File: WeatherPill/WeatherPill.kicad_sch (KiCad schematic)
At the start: 24 parts, among them J2 Conn_02x08_Odd_Even, J3 USB4125-GF-A_REVA2, J4 Conn_02x08_Odd_Even, SW1 EVQ-P7A01P, SW2 EVQ-P7A01P, U1 STM32L052K8Tx, U12 USBLC6-2SC6, U13 BU9796AMUV-E2, U14 SHTC3, U2 SHT40-AD1B-R2, U3 BME280, U4 sst25vf512a-33-4c-sae, U7 STTS22HTR

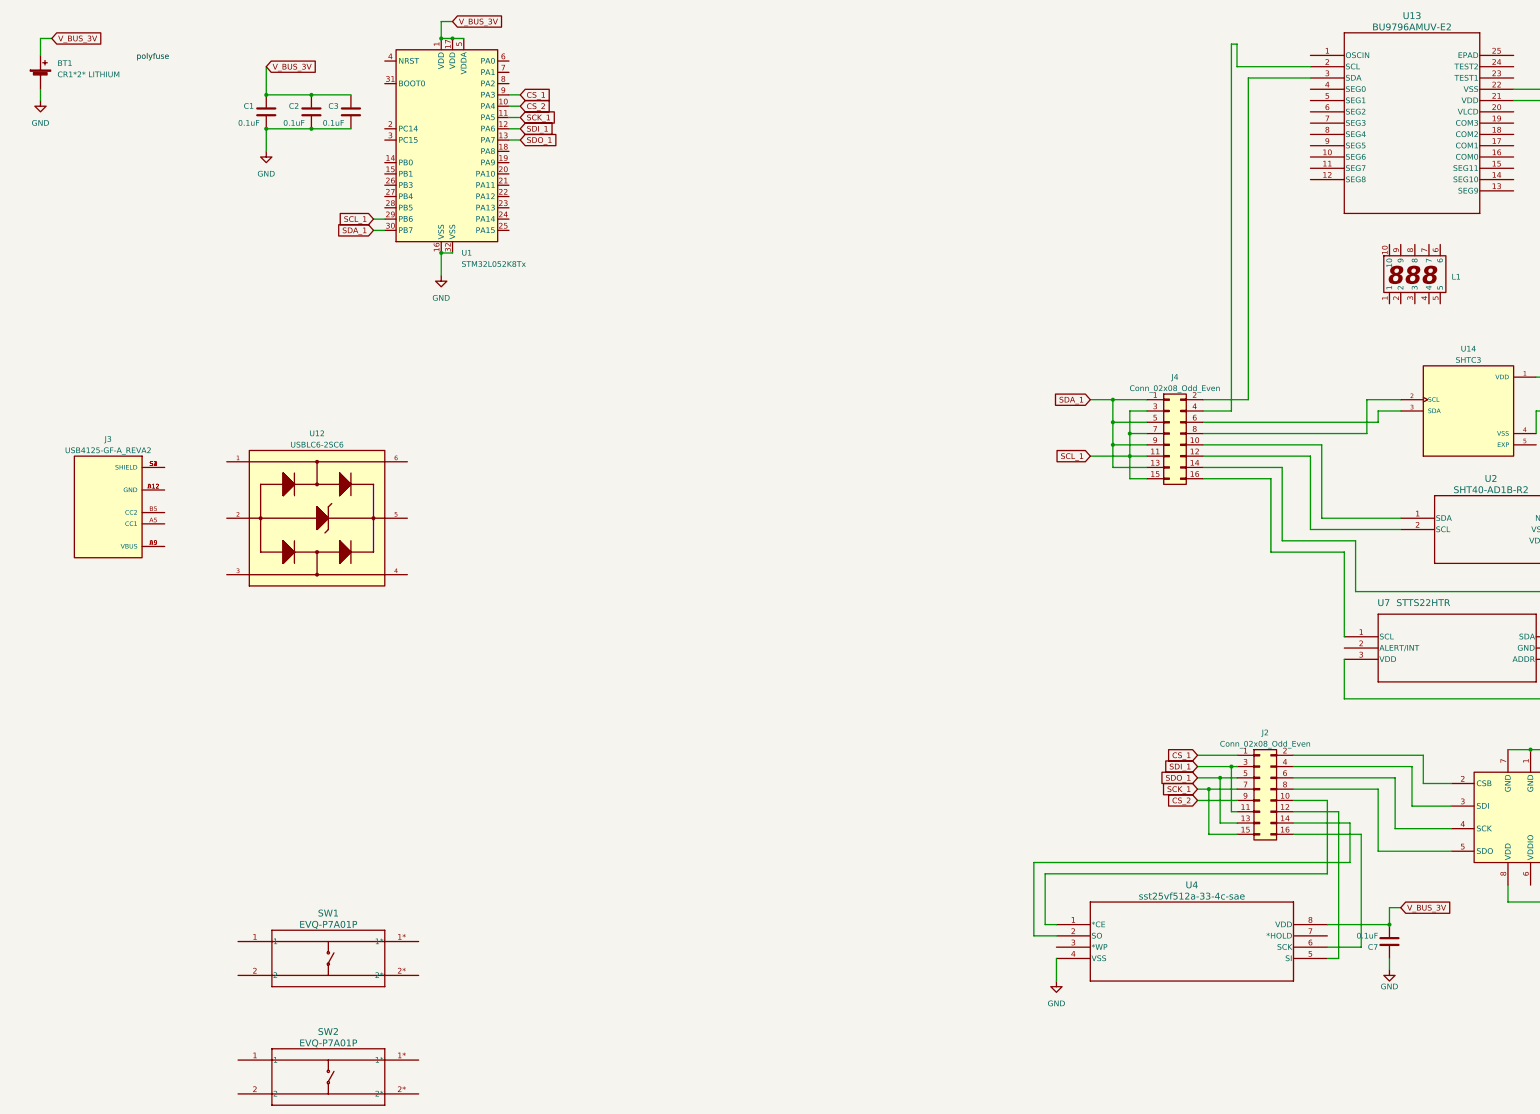
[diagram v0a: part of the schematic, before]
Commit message: stating to configs pins
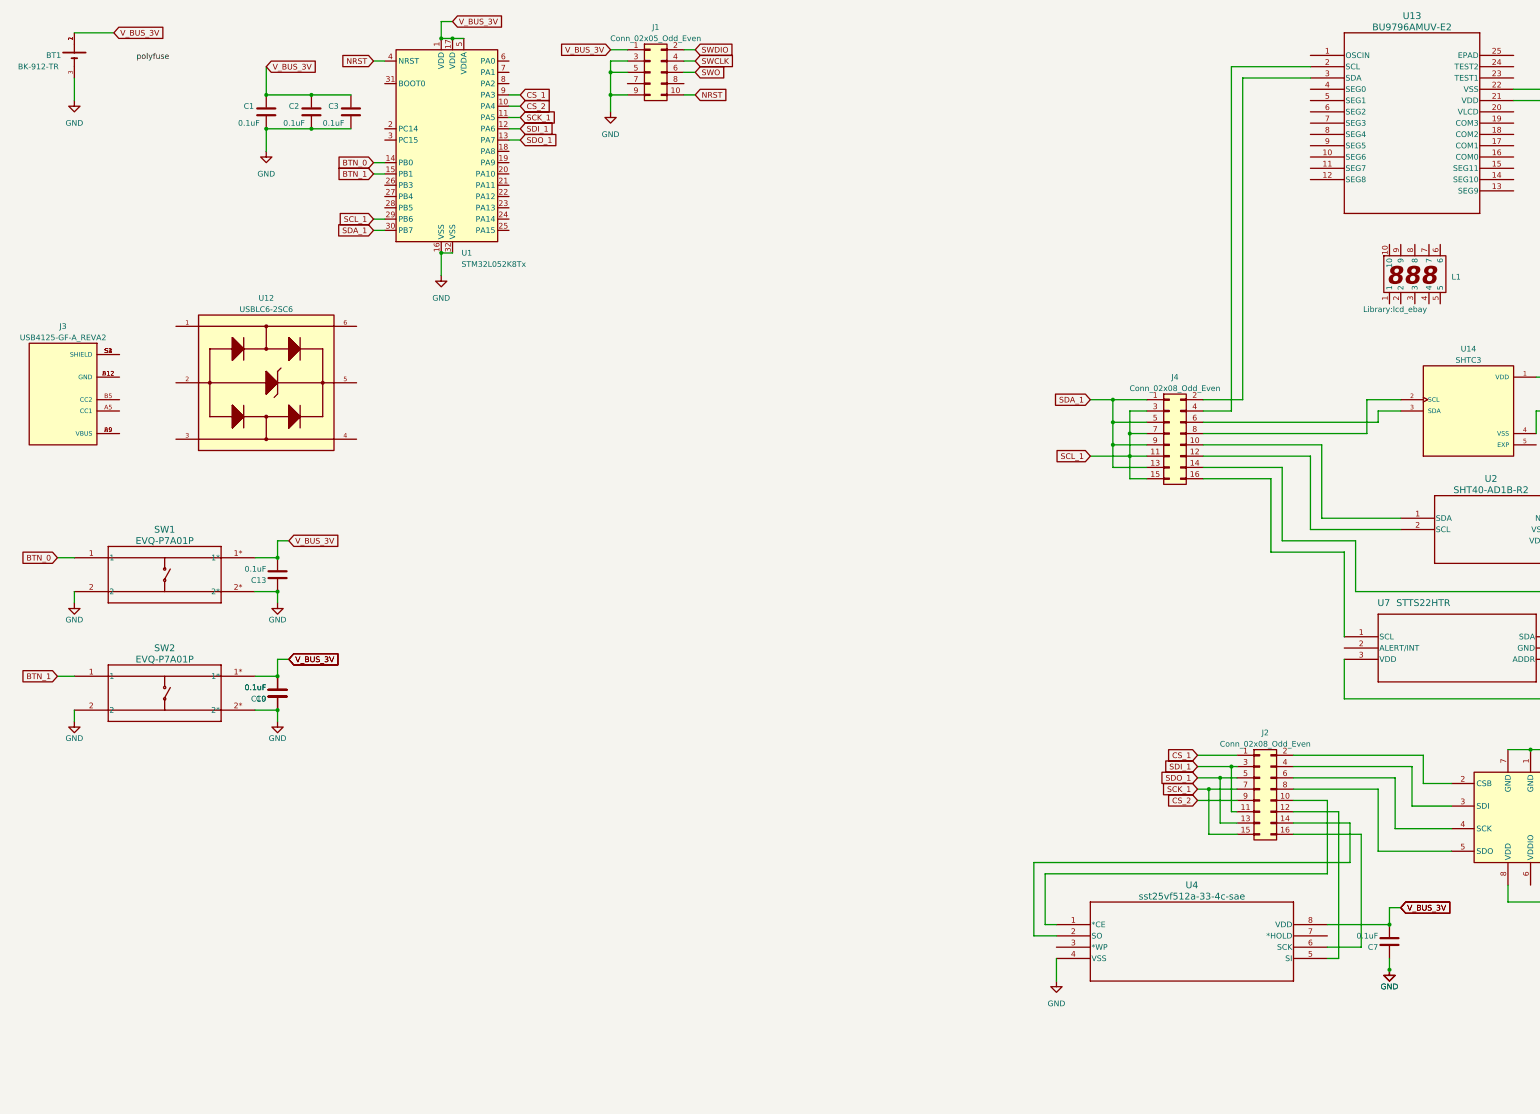
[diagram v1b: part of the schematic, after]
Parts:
- removed BT1: CR1*2* LITHIUM, symbol Device:Battery_Cell
- added BT1: BK-912-TR, MPD_BK-912-TR, symbol BK-912-TR:BK-912-TR
- added C10, C13, C9: 0.1uF, Capacitor_SMD:C_0603_1608Metric_Pad1.08x0.95mm_HandSolder, symbol Device:C
- added J1: Conn_02x05_Odd_Even, symbol Connector_Generic:Conn_02x05_Odd_Even
- L1: footprint (none) -> Library:lcd_ebay
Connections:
- net GND: now also SW1.2, SW1.2*, SW2.2, SW2.2*, BT1.3, C10.1, C13.1, C9.1, J1.3 (Pin_3), J1.5 (Pin_5), J1.9 (Pin_9)
- net V_BUS_3V: now also SW1.1*, SW2.1*, BT1.1, BT1.2, C10.2, C13.2, C9.2, J1.1 (Pin_1)
- net BTN_1: now reaches SW2.1
- net BTN_1: now also U1.15 (PB1)
- net BTN_0: now reaches SW1.1
- net BTN_0: now also U1.14 (PB0)
- net NRST: now reaches U1.4 (NRST)
- net NRST: now also J1.10 (Pin_10)
- new net SWCLK: J1.4 (Pin_4)
- new net SWDIO: J1.2 (Pin_2)
- new net SWO: J1.6 (Pin_6)
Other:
- moved on the sheet: J3, SW1, SW2, U12

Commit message: in review
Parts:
- removed C5, C9: 0.1uF, Capacitor_SMD:C_0603_1608Metric_Pad1.08x0.95mm_HandSolder, symbol Device:C
- removed J3: USB4125-GF-A_REVA2, GCT_USB4125-GF-A_REVA2, symbol usb_CONN:USB4125-GF-A_REVA2
- removed U12: USBLC6-2SC6, SOT95P280X145-6N, symbol tvs:USBLC6-2SC6
- removed U7: STTS22HTR, UDFN-6L_2X2X0P5_STM, symbol STTS22HTR:STTS22HTR
- added C8: 100nF, Capacitor_SMD:C_0603_1608Metric_Pad1.08x0.95mm_HandSolder, symbol Device:C
- added H1, H2, H3, H4: MountingHole, MountingHole:MountingHole_3.2mm_M3_DIN965, symbol Mechanical:MountingHole
- added J3: 12402012E212A, usb conn:12402012E212A_AMP, symbol usb conn:12402012E212A
- added J5: Conn_01x02_Pin, Connector_PinHeader_2.54mm:PinHeader_1x02_P2.54mm_Vertical, symbol Connector:Conn_01x02_Pin
- added Q1, Q2, Q3: PMOS, Package_TO_SOT_SMD:SOT-323_SC-70_Handsoldering, symbol Simulation_SPICE:PMOS
- added R1, R2, R7, R8, R9: 1M, Capacitor_SMD:C_0603_1608Metric_Pad1.08x0.95mm_HandSolder, symbol Device:R
- added R10, R11, R12, R5: 0R, Capacitor_SMD:C_0603_1608Metric_Pad1.08x0.95mm_HandSolder, symbol Device:R
- added R3, R4, R6: 10K, Capacitor_SMD:C_0603_1608Metric_Pad1.08x0.95mm_HandSolder, symbol Device:R
- added SW3, SW4: SW_DPDT_x2, dpdt_switch:450404015514, symbol Switch:SW_DPDT_x2
- added U5: USBLC6-2SC6, Package_TO_SOT_SMD:SOT-23-6, symbol Power_Protection:USBLC6-2SC6
- BT1: footprint MPD_BK-912-TR -> BK-912-TR:MPD_BK-912-TR
- C10, C11, C13, C4, C6: value 0.1uF -> 100nF
- J1: footprint (none) -> Connector_PinSocket_2.54mm:PinSocket_2x05_P2.54mm_Vertical
- SW1, SW2: footprint EVQ_P7_PAN -> button EVQ:EVQ_P7_PAN
- U13: footprint VQFN024V4040_ROM -> lcd driver:VQFN024V4040_ROM
- U14: footprint SON100P200X200X80-5N -> SHT3:SON100P200X200X80-5N
- U2: footprint SHT4x_SEN -> SHT4x_SEN:SHT4x_SEN
- U4: footprint SOIC8_SA_SST_MCH -> sst25vf5:SOIC8_SA_SST_MCH
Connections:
- net BTN_1: now also SW1.1, U1.19 (PA9); no longer SW2.1, U1.15 (PB1)
- net GND: now also U1.14 (PB0), U1.15 (PB1), U1.2 (PC14), U1.20 (PA10), U1.25 (PA15), U1.3 (PC15), U1.6 (PA0), U1.7 (PA1), U1.8 (PA2), U13.20 (VLCD), J5.2 (Pin_2), R10.2, R11.1, R12.2, R5.2, SW3.3 (C)
- net SCL_1: now also R3.1
- net SDA_1: now also R4.1
- net SWCLK: now also U1.24 (PA14)
- net SWDIO: now also U1.23 (PA13)
- net V_BUS_3V: now also Q1.3 (S), Q2.3 (S), Q3.3 (S), R1.2, R2.2, R3.2, R4.2, R7.1, R8.1, R9.1, SW3.1 (A), SW4.1 (A); no longer BT1.1, BT1.2, C10.2, C11.2, C12.2, C13.2, C4.2, C6.2, C7.2, J1.1 (Pin_1), SW1.1*, SW2.1*, U13.21 (VDD), U14.1 (VDD), U2.3 (VDD), U3.8 (VDD), U4.8 (VDD)
- net CS_BME280: now reaches J2.2 (Pin_2), U3.2 (CSB)
- net SDI_BME280: now reaches J2.4 (Pin_4), U3.3 (SDI)
- net SCK_BME280: now reaches U3.4 (SCK)
- net SCK_BME280: now also J2.8 (Pin_8); no longer J2.6 (Pin_6)
- net SDO_BME280: now reaches U3.5 (SDO)
- net SDO_BME280: now also J2.6 (Pin_6); no longer J2.8 (Pin_8)
- net at U13.1 (OSCIN): now also R5.1
- net at U13.16 (COM0): now also L1.10 (A)
- net at U13.17 (COM1): now also L1.9 (B)
- net at U13.18 (COM2): now also L1.8 (C)
- net at U13.19 (COM3): now also L1.7 (D)
- net SCL_DISPLAY: now reaches J4.4 (Pin_4), U13.2 (SCL)
- net SDA_DISPLAY: now reaches J4.2 (Pin_2), U13.3 (SDA)
- net at U13.4 (SEG0): now also L1.1 (0)
- net at U13.5 (SEG1): now also L1.2 (1)
- net at U13.6 (SEG2): now also L1.3 (2)
- net at U13.7 (SEG3): now also L1.4 (3)
- net at U13.8 (SEG4): now also L1.5 (4)
- net at U13.9 (SEG5): now also L1.6 (E)
- net CS_SST25: now reaches J2.10 (Pin_10), U4.1 (*CE)
- net SDI_SST25: now reaches J2.12 (Pin_12), U4.5 (SI)
- net SDO_SST25: now reaches J2.14 (Pin_14), U4.2 (SO)
- net SCK_SST25: now reaches J2.16 (Pin_16), U4.6 (SCK)
- net SCL_SHTC3: now reaches J4.8 (Pin_8), U14.2 (SCL)
- net SDA_SHTC3: now reaches J4.6 (Pin_6), U14.3 (SDA)
- net SDA_SHT40: now reaches J4.10 (Pin_10), U2.1 (SDA)
- net SCL_SHT40: now reaches J4.12 (Pin_12), U2.2 (SCL)
- net at U4.3 (*WP): now also R11.2
- net at U4.7 (*HOLD): now also R12.1
- net BTN_2: now reaches U1.18 (PA8)
- net BTN_2: now also SW2.1
- net USB_D-: now reaches U1.21 (PA11)
- net USB_D-: now also C8.2, U5.6 (I/O1)
- net USB_D+: now reaches U1.22 (PA12)
- net USB_D+: now also C8.1, U5.4 (I/O2)
- net CONTROL_ZONE_3: now reaches U1.26 (PB3)
- net CONTROL_ZONE_3: now also Q3.2 (G), R9.2
- net CONTROL_ZONE_2: now reaches U1.27 (PB4)
- net CONTROL_ZONE_2: now also Q2.2 (G), R8.2
- net CONTROL_ZONE_1: now reaches U1.28 (PB5)
- net CONTROL_ZONE_1: now also Q1.2 (G), R7.2
- net BOOT: now reaches U1.31 (BOOT0)
- net BOOT: now also R6.1
- removed net BTN_0: SW1.1, U1.14 (PB0)
- new net: BT1.1, BT1.2, J5.1 (Pin_1), SW4.2 (B)
- new net: J3.A7 (D-), J3.B7 (D-), U5.1 (I/O1)
- new net: J3.A1-B12 (GND), J3.B1-A12 (GND), R10.1, U5.2 (GND)
- new net: J3.A6 (D+), J3.B6 (D+), U5.3 (I/O2)
- new net: J3.A4-B9 (VBUS), J3.B4-A9 (VBUS), U5.5 (VBUS)
- new net: C13.2, R2.1, SW1.1*
- new net: C10.2, R1.1, SW2.1*
- new net: R6.2, SW3.2 (B)
- new net POWER_IN: J1.1 (Pin_1)
- new net V_BUS_ZONE_1: C7.2, Q1.1 (D), U4.8 (VDD)
- new net V_BUS_ZONE_2: C12.2, C4.2, C6.2, Q2.1 (D), U14.1 (VDD), U2.3 (VDD), U3.8 (VDD)
- new net V_BUS_ZONE_3: C11.2, Q3.1 (D), U13.21 (VDD)
- no-connect marks 0 -> 1
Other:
- note added: "BATTERY"
- note added: "BTN1"
- note added: "BTN2"
- note added: "BUTTONS"
- note added: "DFU/DEBUG"
- note added: "DISPLAY"
- note added: "Humidity"
- note added: "I2C"
- note added: "I2C ADDR : 0x70"
- note added: "MEMORY"
- note added: "Pressure"
- note added: "SENSOR 1"
- note added: "SENSOR 2"
- note added: "SENSOR 3"
- note added: "SPI"
- note added: "STM32"
- note added: "Temperature"
- note added: "USB"
- note added: "ZONES PWR"
- moved on the sheet: BT1, C1, C10, C11, C12, C13, C2, C3, C4, C6, C7, J1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

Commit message: roasting
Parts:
- added R13, R14, R15, R16, R17: 0R, Capacitor_SMD:C_0603_1608Metric_Pad1.08x0.95mm_HandSolder, symbol Device:R
- C1, C2, C3: value 0.1uF -> 100nF
- J3: footprint usb conn:12402012E212A_AMP -> 12402012E212A_AMP
- R3, R4: value 10K -> 47k
- R6: value 10K -> 1M
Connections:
- net GND: now also U14.5 (EXP), R14.2, R15.2, R16.2, R17.2; no longer R11.1, U1.14 (PB0), U1.15 (PB1), U1.2 (PC14), U1.3 (PC15)
- net V_BUS_ZONE_1: now also R11.1
- net at R10.1, U5.2 (GND): now also J3.A1_B12 (GND), J3.B1_A12 (GND); no longer J3.A1-B12 (GND), J3.B1-A12 (GND)
- net at J3.A5 (CC1): now also R13.1
- net at J3.B5 (CC1): now also R13.2
- new net: J3.A4_B9 (VBUS), J3.B4_A9 (VBUS), U5.5 (VBUS)
- new net: R16.1, U1.14 (PB0)
- new net: R15.1, U1.3 (PC15)
- new net: R17.1, U1.15 (PB1)
- new net: R14.1, U1.2 (PC14)

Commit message: revision 2
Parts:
- removed C12: 0.1uF, Capacitor_SMD:C_0603_1608Metric_Pad1.08x0.95mm_HandSolder, symbol Device:C
- removed C4: 100nF, Capacitor_SMD:C_0603_1608Metric_Pad1.08x0.95mm_HandSolder, symbol Device:C
- removed J1: Conn_02x05_Odd_Even, Connector_PinSocket_2.54mm:PinSocket_2x05_P2.54mm_Vertical, symbol Connector_Generic:Conn_02x05_Odd_Even
- removed J4: Conn_02x08_Odd_Even, Connector_PinHeader_2.54mm:PinHeader_2x08_P2.54mm_Vertical_SMD, symbol Connector_Generic:Conn_02x08_Odd_Even
- removed Q3: PMOS, Package_TO_SOT_SMD:SOT-323_SC-70_Handsoldering, symbol Simulation_SPICE:PMOS
- removed R13: 0R, Capacitor_SMD:C_0603_1608Metric_Pad1.08x0.95mm_HandSolder, symbol Device:R
- removed R7, R8: 1M, Capacitor_SMD:C_0603_1608Metric_Pad1.08x0.95mm_HandSolder, symbol Device:R
- removed U14: SHTC3, SHT3:SON100P200X200X80-5N, symbol SHTC3:SHTC3
- removed U2: SHT40-AD1B-R2, SHT4x_SEN:SHT4x_SEN, symbol SHT4x_SEN:SHT40-AD1B-R2
- added J3: Conn_02x04_Odd_Even, Connector_PinSocket_2.54mm:PinSocket_2x04_P2.54mm_Vertical, symbol Connector_Generic:Conn_02x04_Odd_Even
- added J4: Conn_02x05_Odd_Even, Connector_PinHeader_2.54mm:PinHeader_2x05_P2.54mm_Vertical, symbol Connector_Generic:Conn_02x05_Odd_Even
- added R1, R17, R18, R19, R20: 0R, Capacitor_SMD:C_0603_1608Metric_Pad1.08x0.95mm_HandSolder, symbol Device:R
- added R10: 1M, Capacitor_SMD:C_0603_1608Metric_Pad1.08x0.95mm_HandSolder, symbol Device:R
- BT1: footprint BK-912-TR:MPD_BK-912-TR -> bk-912-tr:MPD_BK-912-TR
- J2: renamed from J3; footprint 12402012E212A_AMP -> USB12402012E212A:AMPHENOL_12402012E212A
- J5: renamed from J2; footprint Connector_PinHeader_2.54mm:PinHeader_2x08_P2.54mm_Vertical_SMD -> Connector_PinHeader_2.54mm:PinHeader_2x08_P2.54mm_Vertical
- renumbered C8 to C4, C13 to C5, C10 to C6, C6 to C7, C7 to C8, C11 to C9, J5 to J1, R3 to R11, R4 to R12, R1 to R13, R11 to R14, R5 to R15, R12 to R16, R6 to R2, R10 to R3, R14 to R4, R15 to R5, R16 to R6, R17 to R7, R2 to R8, SW3 to SW1, SW4 to SW2, SW1 to SW3, SW2 to SW4, U5 to U1, U1 to U2, U4 to U3, U13 to U4, U3 to U5
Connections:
- net CONTROL_ZONE_1: now also Q2.2 (G), R10.2; no longer Q1.2 (G)
- net CONTROL_ZONE_2: now also Q1.2 (G), R9.2; no longer Q2.2 (G)
- net GND: now also J3.3 (Pin_3), J3.5 (Pin_5), J3.7 (Pin_7), J4.9 (Pin_9), R1.2, R17.2, R18.1, R19.2, R20.2
- net NRST: now also J3.8 (Pin_8)
- net POWER_IN: now also J3.1 (Pin_1)
- net SCL_1: now also J4.3 (Pin_3)
- net SCL_DISPLAY: now also J4.4 (Pin_4)
- net SDA_1: now also J4.1 (Pin_1)
- net SDA_DISPLAY: now also J4.2 (Pin_2)
- net SWCLK: now also J3.4 (Pin_4)
- net SWDIO: now also J3.2 (Pin_2)
- net SWO: now also J3.6 (Pin_6)
- net V_BUS_3V: now also J4.7 (Pin_7), R10.1; no longer R11.2, R12.2
- net V_BUS_ZONE_1: now also C7.2, Q2.1 (D), U5.6 (VDDIO), U5.8 (VDD); no longer Q1.1 (D)
- net V_BUS_ZONE_2: now also Q1.1 (D), R11.2, R12.2, J4.5 (Pin_5); no longer C7.2, Q2.1 (D), U5.8 (VDD)
- net at L1.10, U4.16 (COM0): now also L1.9, U4.17 (COM1)
- net at L1.6, U4.9 (SEG5): now also U4.10 (SEG6), U4.11 (SEG7), U4.12 (SEG8)
- net at L1.7, U4.19 (COM3): now also L1.8, U4.18 (COM2)
- net at J2.A5 (CC1): now also R1.1
- net at J2.A8 (SBU1): now also R19.1
- net at J2.B5 (CC1): now also R17.1
- net at J2.B8 (SBU2): now also R18.2
- net CONTROL_ZONE_3: no longer names the net of U2.26 (PB3)
- net CONTROL_ZONE_3: now also R20.1; no longer R9.2
- net V_BUS_ZONE_3 renamed V_BUS_DISPLAY
- net V_BUS_DISPLAY: now also J4.6 (Pin_6)
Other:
- note removed: "I2C ADDR : 0x70"
- note removed: "SENSOR 1"
- note removed: "SENSOR 2"
- moved on the sheet: BT1, C1, C2, C3, C4, C5, C6, C7, C8, C9, H1, H2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

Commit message: fred: update pcb
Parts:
- removed C9: 100nF, Capacitor_SMD:C_0603_1608Metric_Pad1.08x0.95mm_HandSolder, symbol Device:C
- removed SW1: SW_DPDT_x2, dpdt_switch:450404015514, symbol Switch:SW_DPDT_x2
- added C10: 100nF, Capacitor_SMD:C_0603_1608Metric_Pad1.08x0.95mm_HandSolder, symbol Device:C
- added JP1: SolderJumper_3_Open, Jumper:SolderJumper-3_P1.3mm_Open_Pad1.0x1.5mm_NumberLabels, symbol Jumper:SolderJumper_3_Open
- added R21, R22, R23, R24, R25, R26, R27, R28: 0R, Capacitor_SMD:C_0603_1608Metric_Pad1.08x0.95mm_HandSolder, symbol Device:R
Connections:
- net GND: now also U4.25 (EPAD), C10.2, JP1.3 (B), R21.1, R22.1, R23.1, R24.1, R25.1; no longer U4.20 (VLCD)
- net V_BUS_3V: now also JP1.1 (A)
- net V_BUS_DISPLAY: now also U4.20 (VLCD), C10.1
- net at R2.2: now also JP1.2 (C)
- net at U4.13 (SEG9): now also R24.2
- net at U4.14 (SEG10): now also R23.2
- net at U4.15 (SEG11): now also R25.2
- net at U4.23 (TEST1): now also R22.2
- net at U4.24 (TEST2): now also R21.2
- new net: R28.1, U4.9 (SEG5)
- new net: L1.6, R26.2, R27.2, R28.2, U4.12 (SEG8)
- new net: R27.1, U4.10 (SEG6)
- new net: R26.1, U4.11 (SEG7)
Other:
- moved on the sheet: J4, Q1, R11, R12, R2, R9, U4

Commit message: fred: avancements
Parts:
- removed R4: 0R, Capacitor_SMD:C_0603_1608Metric_Pad1.08x0.95mm_HandSolder, symbol Device:R
- added D1, D2, D3: LTST-C190GKT, green led:LEDM1608X80, symbol green led:LTST-C190GKT
- added R29, R30, R31: 240R, Resistor_SMD:R_0603_1608Metric_Pad0.98x0.95mm_HandSolder, symbol Device:R_Small
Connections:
- net GND: now also D1.C, D2.C, D3.C
- net V_BUS_ZONE_1: now also R30.1
- net V_BUS_ZONE_2: now also R31.1
- net LED0: now reaches U2.2 (PC14)
- net LED0: now also R29.1
- new net: D3.A, R31.2
- new net: D1.A, R29.2
- new net: D2.A, R30.2
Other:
- moved on the sheet: Q2, R10
